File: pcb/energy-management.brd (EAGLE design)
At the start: 113.3 x 53.7 mm, 79 parts, among them IC2 74LS595D, IC3 74LS595D, J1 WIRE_HOLE-14AWG, J2 WIRE_HOLE-14AWG, J3 WIRE_HOLE-14AWG, J4 WIRE_HOLE-14AWG, U1 DS1307

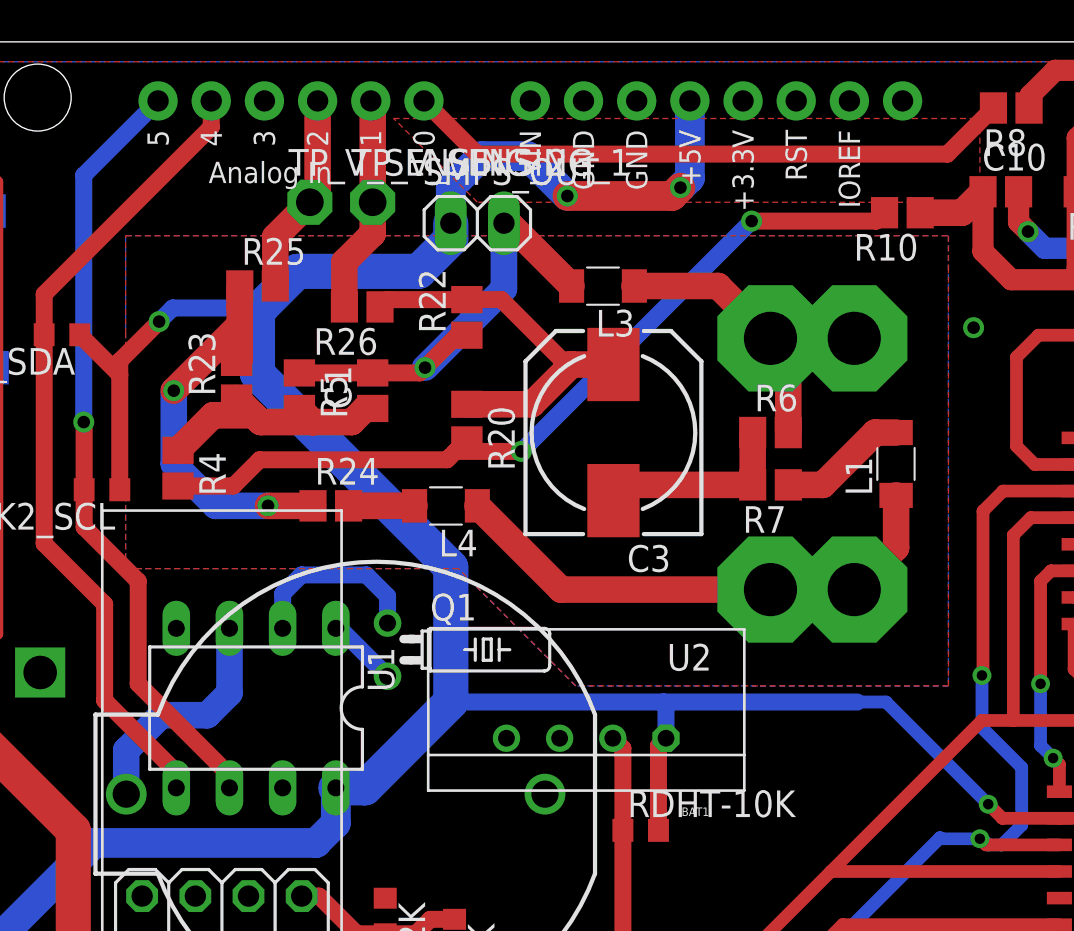
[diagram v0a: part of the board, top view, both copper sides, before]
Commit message: remove unnecessary sensing 2 circuit
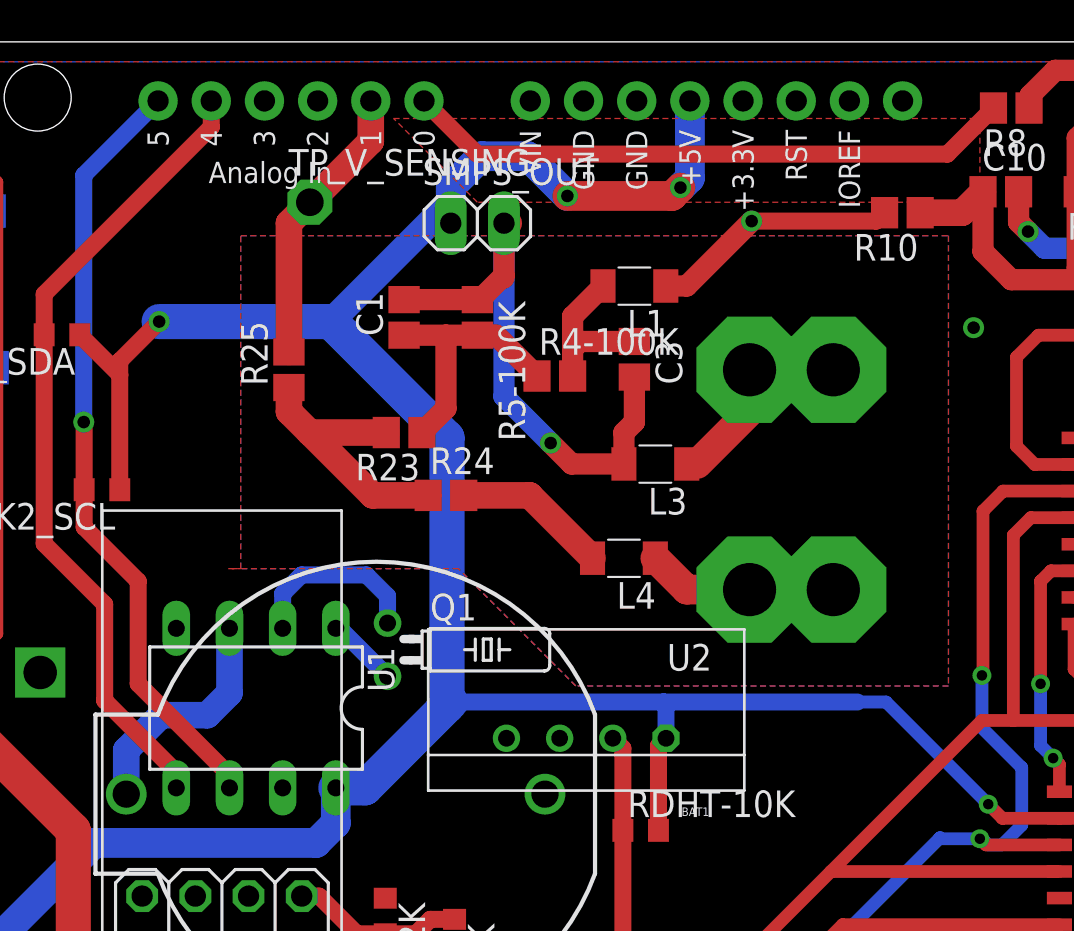
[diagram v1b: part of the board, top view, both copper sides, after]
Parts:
- removed R20, R22, R4, R5: R470K, resistor:R0805
- removed R26, R6: R1K, resistor:R0805
- removed R7: R499K, resistor:R0805
- removed TP_V_SENSING_1: PTR1PAD1-13, testpad:P1-13
- added R4-100K, R5-100K: (no value), resistor:R0805
- C3: value (none) -> C10uF; device resistor:140CLH-0810 -> resistor:C0805
- moved L1 15.1 mm to (71.5, 42.0), turned to 180 degrees
- moved L3 8.86 mm to (72.5, 33.5)
- moved L4 8.86 mm to (71.0, 29.0)
- moved R23 8.38 mm to (60.5, 35.0), turned to 180 degrees
- moved R24 5.52 mm to (62.5, 32.0)
- moved R25 4.27 mm to (55.0, 38.0), turned to 90 degrees
- moved C1 3.81 mm to (60.5, 40.5)
- moved C3 3.64 mm to (71.5, 38.5), turned to 270 degrees
- moved J1 1.80 mm to (77.0, 38.0)
- moved J4 1.80 mm to (81.0, 38.0)
- moved J2 1.00 mm to (77.0, 27.5)
- moved J3 1.00 mm to (81.0, 27.5)
- renumbered TP_V_SENSING_2 to TP_V_SENSING
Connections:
- removed net N$18: L1.2, R7.1
- removed net N$24: C3.+, R20.1, R22.2, R26.1
- removed net V_SENSING_1: R26.2, TP_V_SENSING_1.TP, U$1.A1
- removed net V_SENSING_2: R25.2, TP_V_SENSING.TP, U$1.A2
- new net V_SENSING: R25.2, TP_V_SENSING.TP, U$1.A1
- net 3V3: now also L1.1; no longer R20.2, R4.2
- net GND: now also C3.2, R5-100K.1; no longer R22.1, R5.1
- net N$1: now also C3.1, L1.2, R4-100K.2; no longer C3.-, R6.1, R7.2
- net N$20: now also R4-100K.1, R5-100K.2; no longer R4.1, R5.2
- net WALL_NEUTRAL: no longer R6.2
- net WALL_PHASE: no longer L1.1
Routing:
- net 3V3: track 39.9 -> 11.9 mm, vias 2 -> 1
- net N$24: track 18.4 -> 0.00 mm
- net WALL_PHASE: track 25.0 -> 9.12 mm
- net V_SENSING: track 0.00 -> 13.7 mm
- net V_SENSING_1: track 10.4 -> 0.00 mm
- net V_SENSING_2: track 9.68 -> 0.00 mm
- net N$18: track 6.19 -> 0.00 mm
- net GND: track 69.2 -> 75.3 mm
- net N$21: track 19.1 -> 13.1 mm, vias 2 -> 0
- net WALL_NEUTRAL: track 16.4 -> 10.9 mm
- net N$22: track 3.15 -> 7.39 mm
- net VCC: track 288.5 -> 286.9 mm
- net N$1: track 9.46 -> 8.00 mm

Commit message: change route
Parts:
- moved L4 1.50 mm to (71.0, 27.5)
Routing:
- net N$22: track 7.39 -> 8.01 mm
- net WALL_PHASE: track 9.12 -> 8.50 mm
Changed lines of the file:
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@@
 <element name="R23" library="resistor" package="R0805" value="R1K" x="60.5" y="35" rot="R180"/>
 <element name="R24" library="resistor" package="R0805" value="R499K" x="62.5" y="32"/>
-<element name="L4" library="resistor" package="L3216C" value="BLM31PG330SN1" x="71" y="29" rot="R180"/>
+<element name="L4" library="resistor" package="L3216C" value="BLM31PG330SN1" x="71" y="27.5" rot="R180"/>
 <element name="R25" library="resistor" package="R0805" value="R1K" x="55" y="38" rot="R90"/>
 <element name="TP_V_SENSING" library="testpad" package="P1-13" value="PTR1PAD1-13" x="56" y="46">
@@
 <via x="67.5" y="34.5" extent="1-16" drill="0.6"/>
 <wire x1="67.5" y1="34.5" x2="65.27" y2="36.73" width="1.016" layer="16"/>
-<wire x1="64" y1="41.35" x2="64.12" y2="41.35" width="0" layer="19" extent="1-1"/>
 <wire x1="71.5" y1="37.65" x2="71.5" y2="35.5" width="1.016" layer="1"/>
 <wire x1="71.5" y1="35.5" x2="71" y2="35" width="1.016" layer="1"/>
 <wire x1="71" y1="35" x2="71" y2="33.5" width="1.016" layer="1"/>
+<wire x1="64.12" y1="41.35" x2="64" y2="41.35" width="0" layer="19" extent="1-1"/>
 </signal>
 <signal name="GPIO11">
@@
 <contactref element="J2" pad="P$1"/>
 <contactref element="J3" pad="P$1"/>
-<wire x1="72.5" y1="29" x2="74" y2="27.5" width="1.4224" layer="1"/>
-<wire x1="74" y1="27.5" x2="77" y2="27.5" width="1.4224" layer="1"/>
+<wire x1="72.5" y1="27.5" x2="77" y2="27.5" width="1.4224" layer="1"/>
 <wire x1="77" y1="27.5" x2="81" y2="27.5" width="1.4224" layer="1"/>
 </signal>
@@
 <wire x1="66.85" y1="37.7" x2="64.9" y2="39.65" width="1.016" layer="1"/>
 <wire x1="64.9" y1="39.65" x2="64" y2="39.65" width="1.016" layer="1"/>
-<wire x1="64" y1="39.65" x2="62.5" y2="39.65" width="1.016" layer="1"/>
-<wire x1="62.5" y1="39.65" x2="60.5" y2="39.65" width="1.016" layer="1"/>
-<wire x1="61.35" y1="35" x2="62.5" y2="36.15" width="1.016" layer="1"/>
-<wire x1="62.5" y1="36.15" x2="62.5" y2="39.65" width="1.016" layer="1"/>
+<wire x1="61.35" y1="35" x2="62.425" y2="36.075" width="1.016" layer="1"/>
+<wire x1="62.425" y1="36.075" x2="62.5" y2="36.15" width="1.016" layer="1"/>
+<wire x1="60.5" y1="39.65" x2="62.425" y2="37.725" width="1.27" layer="1"/>
+<wire x1="62.425" y1="37.725" x2="62.425" y2="36.5" width="1.27" layer="1"/>
+<wire x1="62.425" y1="36.5" x2="62.425" y2="36.075" width="1.27" layer="1"/>
+<wire x1="64" y1="39.65" x2="62.425" y2="38.075" width="1.27" layer="1"/>
+<wire x1="62.425" y1="38.075" x2="62.425" y2="37.725" width="1.27" layer="1"/>
 </signal>
 <signal name="N$21">
@@
 <contactref element="R24" pad="2"/>
 <contactref element="L4" pad="2"/>
-<wire x1="69.5" y1="29" x2="66.5" y2="32" width="1.27" layer="1"/>
-<wire x1="66.5" y1="32" x2="63.35" y2="32" width="1.27" layer="1"/>
+<wire x1="63.35" y1="32" x2="67.85" y2="27.5" width="1.27" layer="1"/>
+<wire x1="67.85" y1="27.5" x2="69.5" y2="27.5" width="1.27" layer="1"/>
 </signal>
 <signal name="AGND" class="2">

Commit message: change route
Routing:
- net GND: vias 24 -> 25
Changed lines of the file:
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@@
 <wire x1="71" y1="35" x2="71" y2="33.5" width="1.016" layer="1"/>
 <wire x1="64.12" y1="41.35" x2="64" y2="41.35" width="0" layer="19" extent="1-1"/>
+<via x="87.7" y="36.51" extent="1-16" drill="0.6"/>
 </signal>
 <signal name="GPIO11">

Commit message: update board
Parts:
- moved LED2 4.00 mm to (35.2, 4.14)
- moved LED1 3.00 mm to (39.9, 4.06)
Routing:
- net N$11: track 2.38 -> 5.96 mm
- net N$8: track 4.35 -> 2.89 mm
- net N$12: track 10.7 -> 10.2 mm
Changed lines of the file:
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@@
 <element name="X1" library="microbuilder" package="SMA90_DIP" value="" x="5.27" y="47.42" rot="R90"/>
 <element name="T1" library="transistor" package="SOT23-BEC" value="" x="36.41" y="12.12" rot="MR180"/>
-<element name="LED1" library="SparkFun-LED" package="LED3MM-NS" value="" x="36.89" y="4.06" rot="R180"/>
+<element name="LED1" library="SparkFun-LED" package="LED3MM-NS" value="" x="39.89" y="4.06" rot="R180"/>
 <element name="R20-1K" library="rcl" package="R0603" value="" x="40.39" y="7.46" rot="MR90"/>
 <element name="R23-1K" library="rcl" package="R0603" value="" x="36.37" y="20.37" rot="MR90"/>
 <element name="R25-10K" library="rcl" package="R0603" value="" x="36.46" y="16.8" rot="MR180"/>
 <element name="T2" library="transistor" package="SOT23-BEC" value="" x="31.31" y="12.08" rot="MR180"/>
-<element name="LED2" library="SparkFun-LED" package="LED3MM-NS" value="" x="31.22" y="4.14"/>
+<element name="LED2" library="SparkFun-LED" package="LED3MM-NS" value="" x="35.22" y="4.14"/>
 <element name="R26-1K" library="rcl" package="R0603" value="" x="30.87" y="6.49" rot="MR180"/>
 <element name="R27-1K" library="rcl" package="R0603" value="" x="31.46" y="20.3" rot="MR90"/>
@@
 <wire x1="71.5" y1="35.5" x2="71" y2="35" width="1.016" layer="1"/>
 <wire x1="71" y1="35" x2="71" y2="33.5" width="1.016" layer="1"/>
+<via x="87.7" y="36.51" extent="1-16" drill="0.6"/>
 <wire x1="64.12" y1="41.35" x2="64" y2="41.35" width="0" layer="19" extent="1-1"/>
-<via x="87.7" y="36.51" extent="1-16" drill="0.6"/>
 </signal>
 <signal name="GPIO11">
@@
 <contactref element="R20-1K" pad="1"/>
 <wire x1="40.39" y1="4.79" x2="40.39" y2="6.61" width="0.6096" layer="16"/>
-<wire x1="40.39" y1="4.79" x2="39.66" y2="4.06" width="0.6096" layer="16"/>
-<wire x1="39.66" y1="4.06" x2="38.16" y2="4.06" width="0.6096" layer="16"/>
+<wire x1="40.39" y1="4.79" x2="41.12" y2="4.06" width="0.6096" layer="16"/>
+<wire x1="41.12" y1="4.06" x2="41.16" y2="4.06" width="0.6096" layer="16"/>
 </signal>
 <signal name="N$9">
 <contactref element="LED1" pad="K"/>
 <contactref element="T1" pad="C"/>
-<wire x1="36.5" y1="4.54" x2="36.5" y2="10.93" width="0.6096" layer="16"/>
 <wire x1="36.5" y1="10.93" x2="36.41" y2="11.02" width="0.6096" layer="16" curve="90"/>
-<wire x1="36.5" y1="4.54" x2="36.02" y2="4.06" width="0.6096" layer="16"/>
-<wire x1="36.02" y1="4.06" x2="35.62" y2="4.06" width="0.6096" layer="16"/>
+<wire x1="36.5" y1="10.93" x2="36.5" y2="7" width="0.6096" layer="16"/>
+<wire x1="36.5" y1="7" x2="38.62" y2="4.88" width="0.6096" layer="16"/>
+<wire x1="38.62" y1="4.88" x2="38.62" y2="4.06" width="0.6096" layer="16"/>
 </signal>
 <signal name="N$10">
@@
 <contactref element="R26-1K" pad="1"/>
 <wire x1="30.02" y1="6.49" x2="29.95" y2="6.42" width="0.8128" layer="16"/>
-<wire x1="29.95" y1="6.42" x2="29.95" y2="4.14" width="0.8128" layer="16"/>
+<wire x1="29.95" y1="6.42" x2="29.95" y2="5.05" width="0.6096" layer="16"/>
+<wire x1="29.95" y1="5.05" x2="31" y2="4" width="0.6096" layer="16"/>
+<wire x1="31" y1="4" x2="33.81" y2="4" width="0.6096" layer="16"/>
+<wire x1="33.81" y1="4" x2="33.95" y2="4.14" width="0.6096" layer="16"/>
 </signal>
 <signal name="N$12">
@@
 <wire x1="33.12" y1="10.98" x2="35" y2="9.1" width="0.8128" layer="16"/>
 <wire x1="35" y1="9.1" x2="35" y2="6.5" width="0.8128" layer="16"/>
-<wire x1="35" y1="6.5" x2="32.64" y2="4.14" width="0.8128" layer="16"/>
-<wire x1="32.64" y1="4.14" x2="32.49" y2="4.14" width="0.8128" layer="16"/>
+<wire x1="35" y1="6.5" x2="35" y2="5.63" width="0.6096" layer="16"/>
+<wire x1="35" y1="5.63" x2="36.49" y2="4.14" width="0.6096" layer="16"/>
 </signal>
 <signal name="N$13">

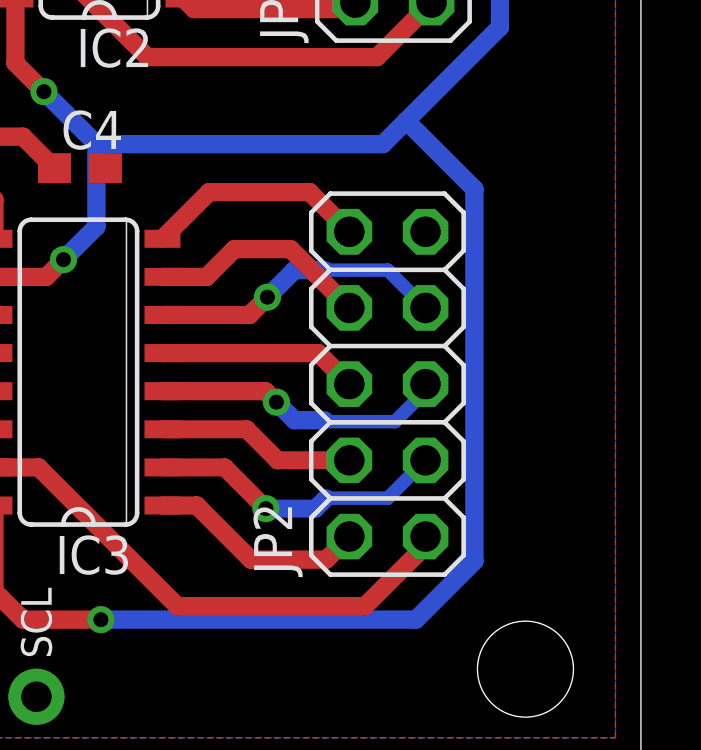
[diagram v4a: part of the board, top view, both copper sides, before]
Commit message: connect vcc to out
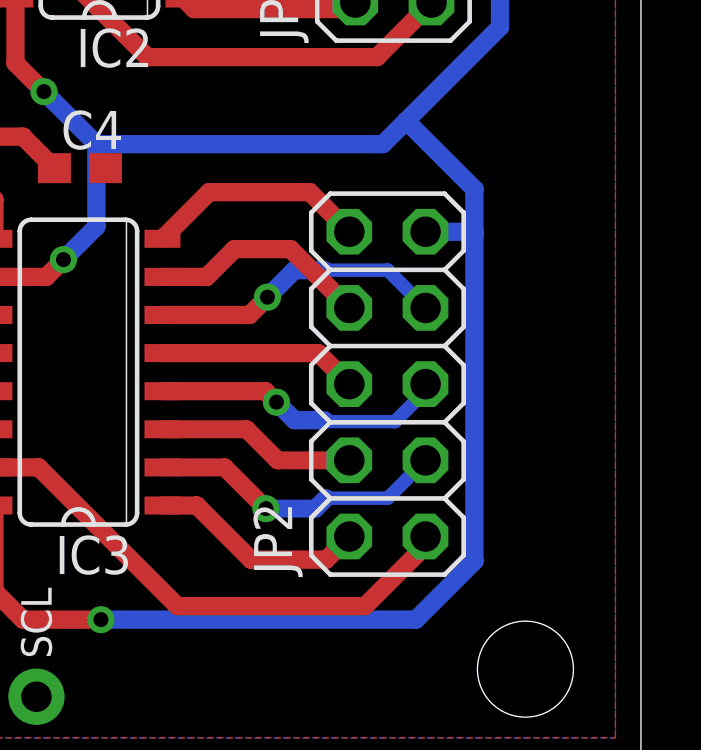
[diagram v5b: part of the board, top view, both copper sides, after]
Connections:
- removed net N$30: JP2.9
- net VCC: now also JP2.9
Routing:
- net VCC: track 286.9 -> 288.5 mm
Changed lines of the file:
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@@
 <wire x1="95.35" y1="5.15" x2="105.85" y2="5.15" width="0.6096" layer="16"/>
 <wire x1="105.85" y1="5.15" x2="107.8" y2="7.1" width="0.6096" layer="16"/>
-<wire x1="107.8" y1="7.1" x2="107.8" y2="19.5" width="0.6096" layer="16"/>
+<wire x1="107.8" y1="7.1" x2="107.8" y2="18" width="0.6096" layer="16"/>
+<wire x1="107.8" y1="18.08" x2="107.8" y2="19.5" width="0.6096" layer="16"/>
 <wire x1="107.8" y1="19.5" x2="105.525" y2="21.775" width="0.6096" layer="16"/>
 <wire x1="91.8" y1="8.955" x2="91.8" y2="6.1" width="0.6096" layer="1"/>
@@
 <wire x1="62.73" y1="46.03" x2="62.73" y2="46.5" width="1.27" layer="16"/>
 <wire x1="62.55" y1="34.75" x2="62.55" y2="21.95" width="1.6764" layer="16"/>
+<contactref element="JP2" pad="9"/>
+<wire x1="106.17" y1="18.08" x2="107.8" y2="18.08" width="0.6096" layer="16"/>
+<wire x1="107.8" y1="18.08" x2="107.8" y2="18" width="0.6096" layer="16"/>
 </signal>
 <signal name="SCL">
@@
 <wire x1="91.8" y1="19.15" x2="91.8" y2="17.845" width="0.6096" layer="1"/>
 </signal>
-<signal name="N$30">
-<contactref element="JP2" pad="9"/>
-</signal>
 <signal name="DHT_DATA">

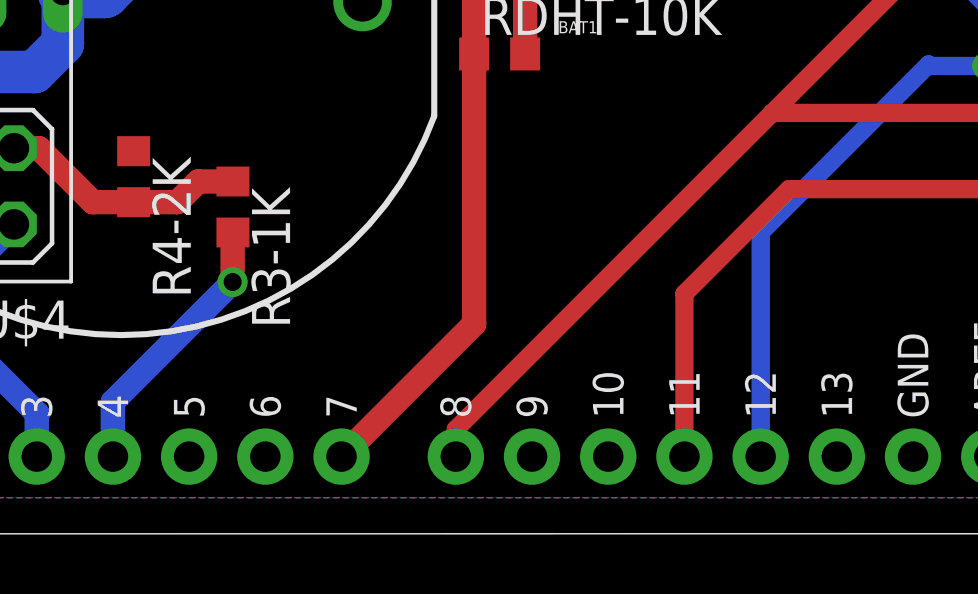
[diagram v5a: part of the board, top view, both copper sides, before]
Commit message: update board
SH_CP and DS cannot be place on Eth pin
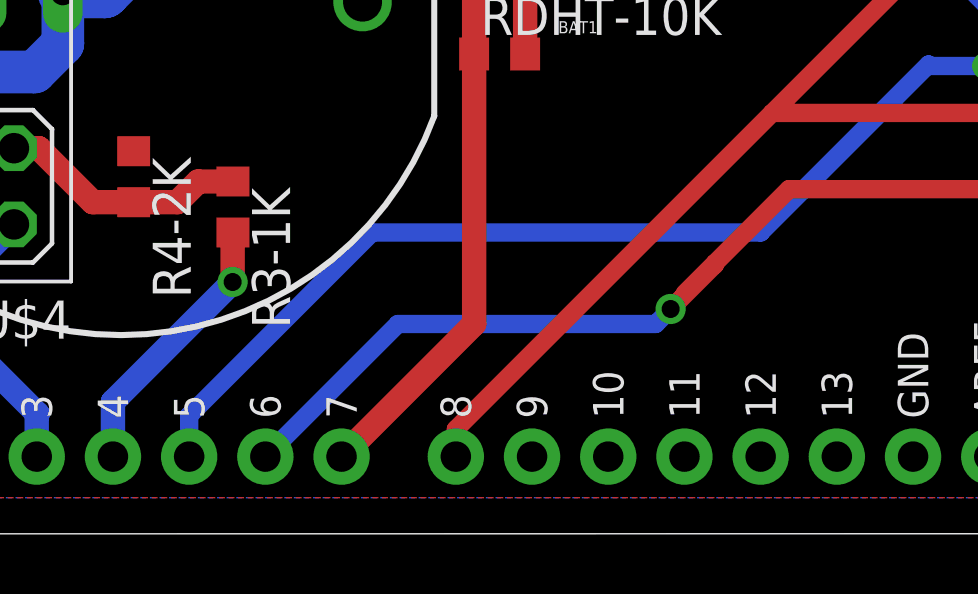
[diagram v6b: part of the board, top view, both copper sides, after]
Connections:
- net DS: now also U$1.D6; no longer U$1.D11
- net SH_CP: now also U$1.D5; no longer U$1.D12
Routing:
- net SH_CP: track 44.3 -> 59.8 mm
- net DS: track 20.7 -> 33.0 mm, vias 0 -> 1
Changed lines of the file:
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@@
 <signal name="DS">
 <contactref element="IC3" pad="14"/>
-<contactref element="U$1" pad="D11"/>
 <wire x1="91.8" y1="11.495" x2="81.445" y2="11.495" width="0.6096" layer="1"/>
-<wire x1="81.445" y1="11.495" x2="77.96" y2="8.01" width="0.6096" layer="1"/>
-<wire x1="77.96" y1="8.01" x2="77.96" y2="2.58" width="0.6096" layer="1"/>
+<wire x1="81.445" y1="11.495" x2="78.975" y2="9.025" width="0.6096" layer="1"/>
+<contactref element="U$1" pad="D6"/>
+<wire x1="78.975" y1="9.025" x2="77.96" y2="8.01" width="0.6096" layer="1"/>
+<wire x1="63.99" y1="2.58" x2="68.41" y2="7" width="0.6096" layer="16"/>
+<wire x1="68.41" y1="7" x2="77" y2="7" width="0.6096" layer="16"/>
+<wire x1="77" y1="7" x2="77.5" y2="7.5" width="0.6096" layer="16"/>
+<via x="77.5" y="7.5" extent="1-16" drill="0.6"/>
+<wire x1="77.5" y1="7.5" x2="78.975" y2="8.975" width="0.6096" layer="1"/>
+<wire x1="78.975" y1="8.975" x2="78.975" y2="9.025" width="0.6096" layer="1"/>
 </signal>
 <signal name="SH_CP">
 <contactref element="IC3" pad="11"/>
 <contactref element="IC2" pad="11"/>
-<contactref element="U$1" pad="D12"/>
-<wire x1="80.5" y1="2.58" x2="80.5" y2="10.05" width="0.6096" layer="16"/>
 <wire x1="80.5" y1="10.05" x2="86.1" y2="15.65" width="0.6096" layer="16"/>
 <wire x1="91.8" y1="15.305" x2="88.295" y2="15.305" width="0.6096" layer="1"/>
@@
 <wire x1="88.4" y1="15.305" x2="88.105" y2="15.6" width="0.6096" layer="16"/>
 <wire x1="88.105" y1="15.6" x2="88" y2="15.6" width="0.6096" layer="16"/>
+<contactref element="U$1" pad="D5"/>
+<wire x1="61.45" y1="2.58" x2="61.45" y2="3.95" width="0.6096" layer="16"/>
+<wire x1="61.45" y1="3.95" x2="67.55" y2="10.05" width="0.6096" layer="16"/>
+<wire x1="67.55" y1="10.05" x2="80.5" y2="10.05" width="0.6096" layer="16"/>
 </signal>
 <signal name="ST_CP">
